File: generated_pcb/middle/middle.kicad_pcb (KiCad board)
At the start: 2 copper layers, 114.5 x 101.2 mm, 102 parts, among them J1 L_B_LED, J2 R_B_LED, J3 SLAVE_LED, P1 OLED, P2 ICSP, SW0:0 SW_Push, SW0:1 SW_Push, SW0:2 SW_Push, SW0:3 SW_Push, SW0:4 SW_Push, SW1:0 SW_Push, SW1:1 SW_Push, SW1:2 SW_Push, SW1:3 SW_Push, SW1:4 SW_Push, SW2:0 SW_Push, SW2:1 SW_Push, SW2:2 SW_Push, SW2:3 SW_Push, SW2:4 SW_Push, SW3:0 SW_Push, SW3:1 SW_Push, SW3:2 SW_Push, SW3:3 SW_Push, SW3:4 SW_Push, SW3:5 SW_Push, SW4:1 SW_Push, SW4:2 SW_Push, SW4:3 SW_Push, SW4:4 SW_Push, SW4:5 SW_Push

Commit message: fix: generating something for all layers, outline is good, zones are refilled, still more to do
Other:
- board text removed: "10. cut switch holes from switch plate 11. install 4 MX switches"
- board text removed: "12. solder switch plate to PCB with diode legs 13. install standoffs"
- board text removed: "14. install remaining switches"
- board text removed: "15. install base plate and feet"
- board text removed: "16. install ProMicro and OLED"
- board text removed: "3. install reset switch 4. install top LED 5a. (optional for OLED) install I2C resistors"
- board text removed: "5b. solder top jumpers 5c. install OLED header"
- board text removed: "6. install ProMicro socket (DO NOT SOLDER PRO MICRO)"
- board text removed: "7. drill standoff holes on PCB 8. install switch sockets"
- board text removed: "9. cut bottom row and ProMicro area off switch plate"
- board text removed: "Build instructions: 1. install diodes 2. install TRRS connector"
- board text removed: "Designed by Tom Saleeba. Copyright 2019 - MIT License"
- board text removed: "ErgoSlab"
- board text removed: "OLED I2C resistors"
- board text removed: "v0.3.0"

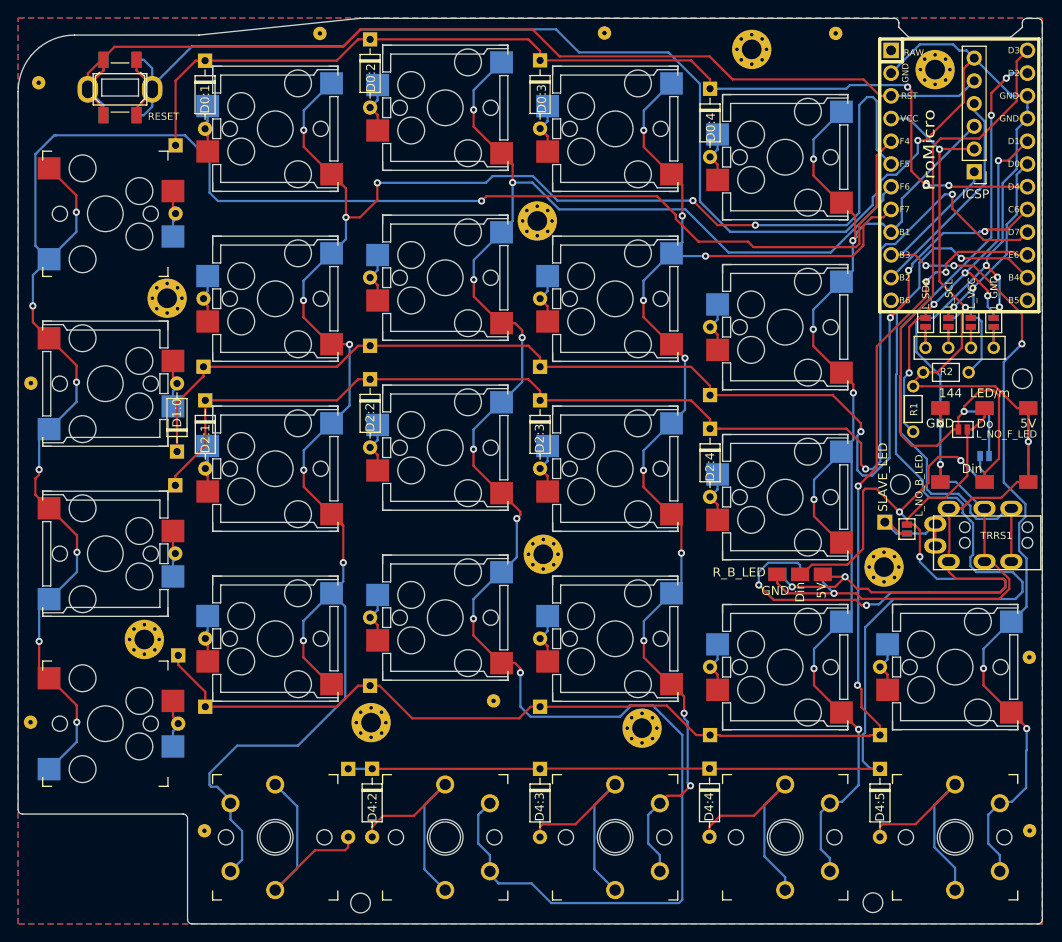
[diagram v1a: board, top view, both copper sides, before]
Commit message: feat: completed the new approach of generating PCBs from the master
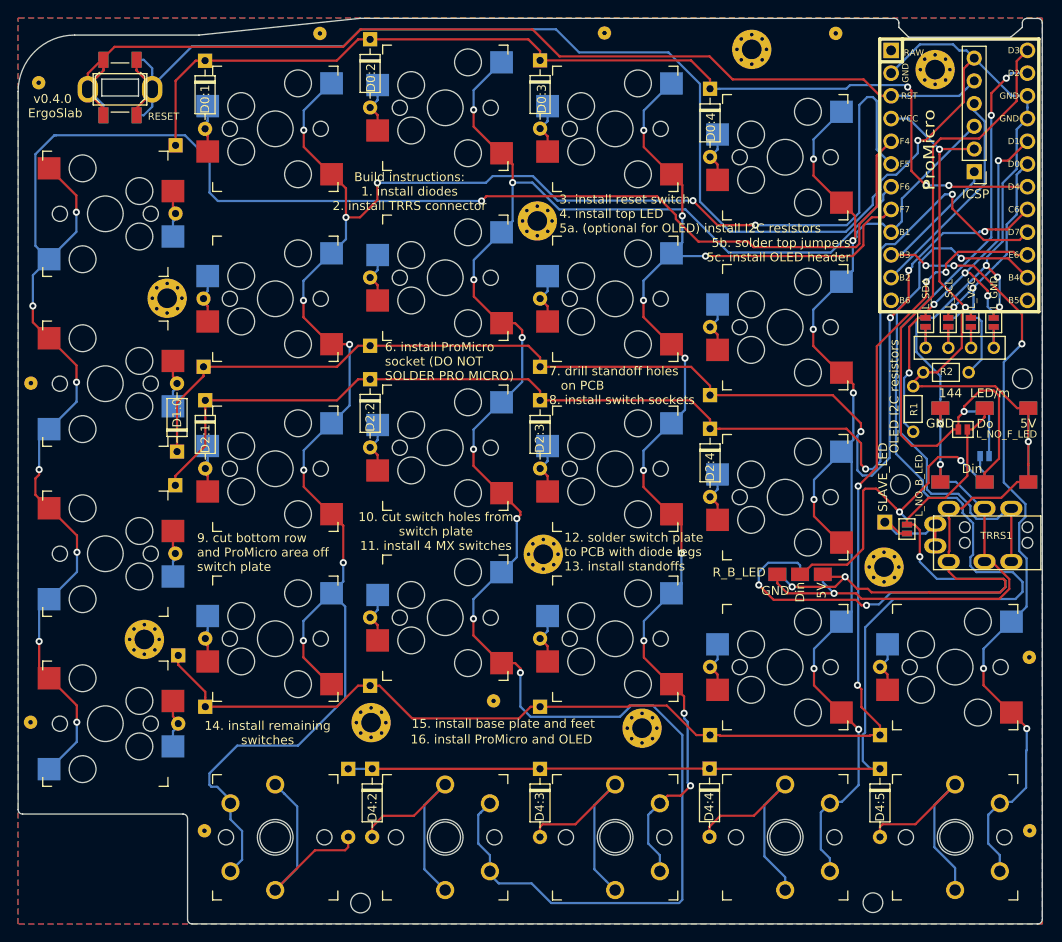
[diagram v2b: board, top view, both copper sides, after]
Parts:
- renumbered BRACE0 to Brace0, BRACE1 to Brace1, BRACE2 to Brace2, BRACE3 to Brace3, BRACE4 to Brace4, BRACE5 to Brace5, BRACE6 to Brace6, BRACE9 to Brace7, BRACE8 to BraceNotTop0, BRACE7 to BraceNotTop1, G*** to CHICKEN, Drill to Mount0, Drill to Mount1, Drill to Mount2, Drill to Mount3, Drill to Mount4, Drill to Mount5, Drill to Mount6, Drill to Mount7, Drill to MountNotTop0, HOLE_M2 to MountNotTop1, HOLE_M2 to MountNotTop2, HOLE_M2 to MountNotTop3, HOLE_M2 to MountNotTop4
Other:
- outline, holes or cut-outs redrawn
- board text added: "10. cut switch holes from switch plate 11. install 4 MX switches"
- board text added: "12. solder switch plate to PCB with diode legs 13. install standoffs"
- board text added: "14. install remaining switches"
- board text added: "15. install base plate and feet"
- board text added: "16. install ProMicro and OLED"
- board text added: "3. install reset switch 4. install top LED 5a. (optional for OLED) install I2C resistors"
- board text added: "5b. solder top jumpers 5c. install OLED header"
- board text added: "6. install ProMicro socket (DO NOT SOLDER PRO MICRO)"
- board text added: "7. drill standoff holes on PCB 8. install switch sockets"
- board text added: "9. cut bottom row and ProMicro area off switch plate"
- board text added: "Build instructions: 1. install diodes 2. install TRRS connector"
- board text added: "Designed by Tom Saleeba. Copyright 2019 - MIT License"
- board text added: "ErgoSlab"
- board text added: "OLED I2C resistors"
- board text added: "v0.4.0"

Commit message: chore: bump version to 1.0.0 now I know it works (typing on it right now), give OLED resistor more space, make choc row M2 mounts more obvious, fix up silk screen build instructions
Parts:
- MountNotTop3, MountNotTop4: value VAL** -> MountingHole_2.2mm_M2_Pad_Via; footprint footprints:HOLE_M2 -> MountingHole:MountingHole_2.2mm_M2_Pad_Via
- moved R2 1.73 mm to (177.9, 83.8)
- turned MountNotTop3 to 270 degrees
- turned MountNotTop4 to 270 degrees
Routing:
- net VCC: track 130.8 -> 131.5 mm
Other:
- board text added: "10. install remaining MX switches"
- board text added: "11. install hotswap sockets and solder"
- board text added: "12. install Choc switches and solder"
- board text added: "13. install ProMicro, base plate and OLED"
- board text added: "3. install top LED 4. install TRRS 5a. (optional for OLED) install I2C resistors"
- board text added: "6. install standoffs"
- board text added: "7. install ProMicro socket (DON'T SOLDER PM)"
- board text added: "8. install 4 mx switches 9. solder diode legs in switch plate braces"
- board text added: "Build instructions: 1. install diodes 2. install reset switch"
- board text added: "GND"
- board text added: "VCC"
- board text added: "v1.0.0"
- board text removed: "10. cut switch holes from switch plate 11. install 4 MX switches"
- board text removed: "12. solder switch plate to PCB with diode legs 13. install standoffs"
- board text removed: "14. install remaining switches"
- board text removed: "15. install base plate and feet"
- board text removed: "16. install ProMicro and OLED"
- board text removed: "3. install reset switch 4. install top LED 5a. (optional for OLED) install I2C resistors"
- board text removed: "6. install ProMicro socket (DO NOT SOLDER PRO MICRO)"
- board text removed: "7. drill standoff holes on PCB 8. install switch sockets"
- board text removed: "9. cut bottom row and ProMicro area off switch plate"
- board text removed: "Build instructions: 1. install diodes 2. install TRRS connector"
- board text removed: "v0.4.0"
